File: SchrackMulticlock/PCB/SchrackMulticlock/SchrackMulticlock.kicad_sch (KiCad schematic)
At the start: 4 parts

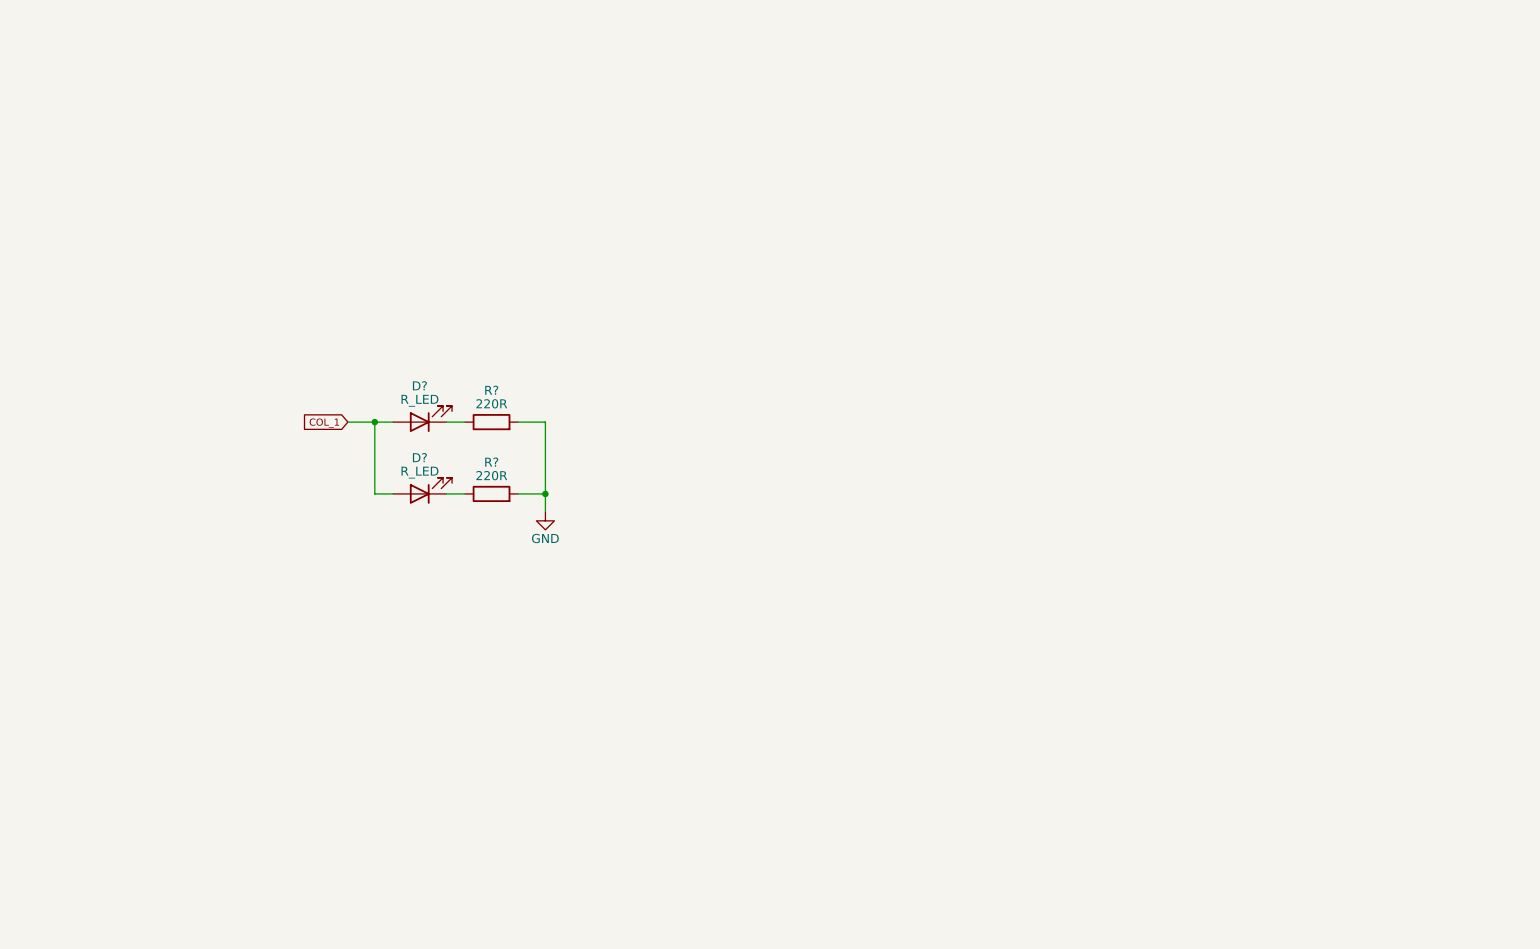
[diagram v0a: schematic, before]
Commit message: SchrackMulticlock update
Start of schematic
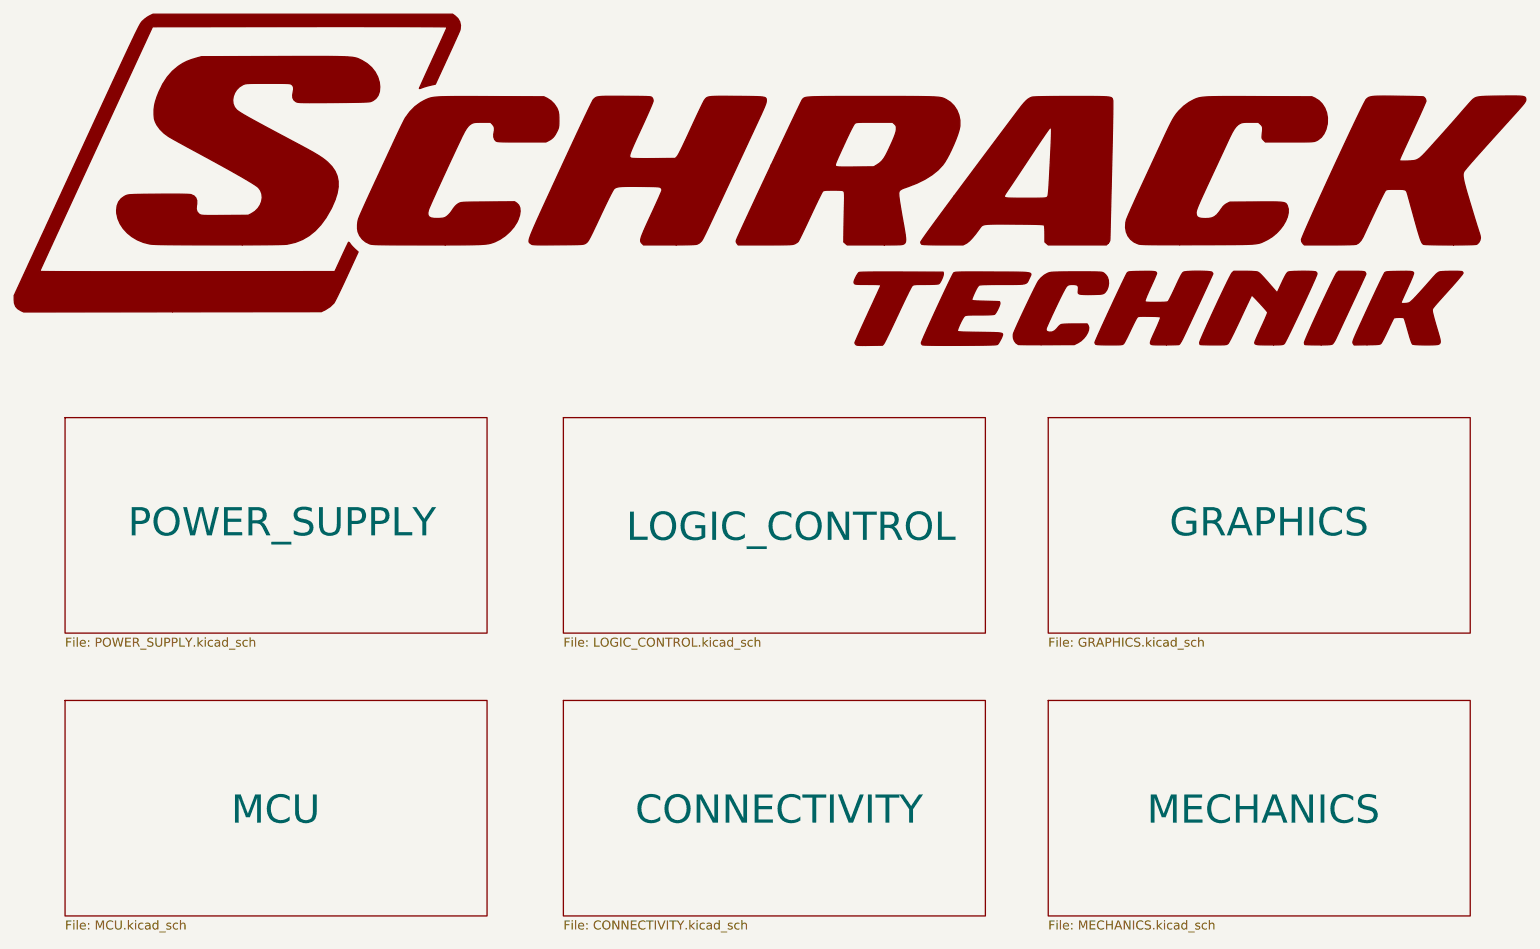
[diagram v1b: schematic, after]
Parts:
- removed D? (x2): R_LED, symbol Device:LED
- removed R? (x2): 220R, symbol Device:R
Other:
- added sheet CONNECTIVITY (CONNECTIVITY.kicad_sch)
- added sheet GRAPHICS (GRAPHICS.kicad_sch)
- added sheet LOGIC_CONTROL (LOGIC_CONTROL.kicad_sch)
- added sheet MCU (MCU.kicad_sch)
- added sheet MECHANICS (MECHANICS.kicad_sch)
- added sheet POWER_SUPPLY (POWER_SUPPLY.kicad_sch)
- company: (none) -> SPS NA PROSEKU
- title: (none) -> SchrackStopwatch
